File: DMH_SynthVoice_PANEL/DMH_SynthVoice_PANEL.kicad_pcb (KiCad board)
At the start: 2 copper layers, 100 x 200 mm, 5 parts, among them J0 Panel_GND_Solder_Wire_Pad

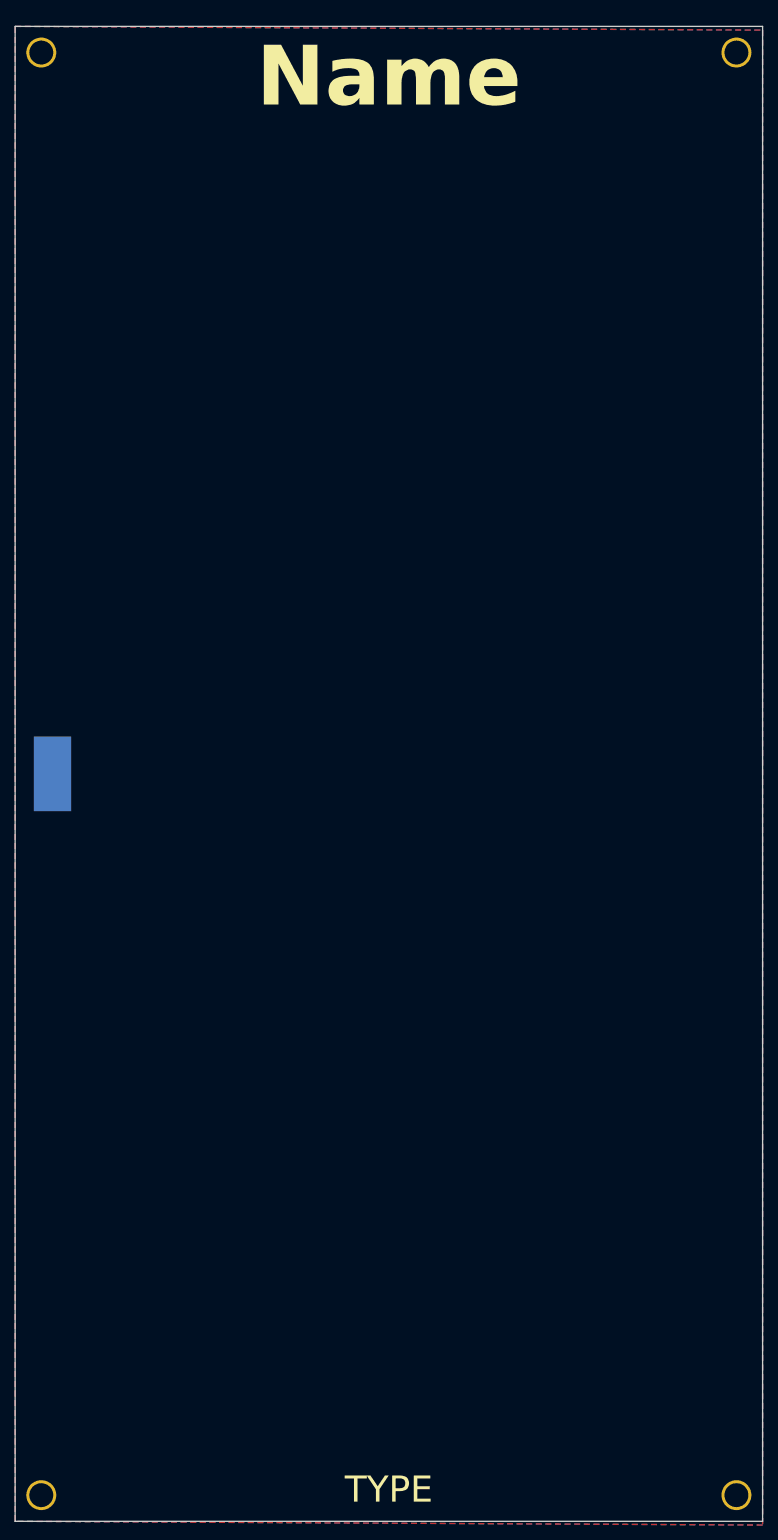
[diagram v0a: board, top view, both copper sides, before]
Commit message: Designed front panel
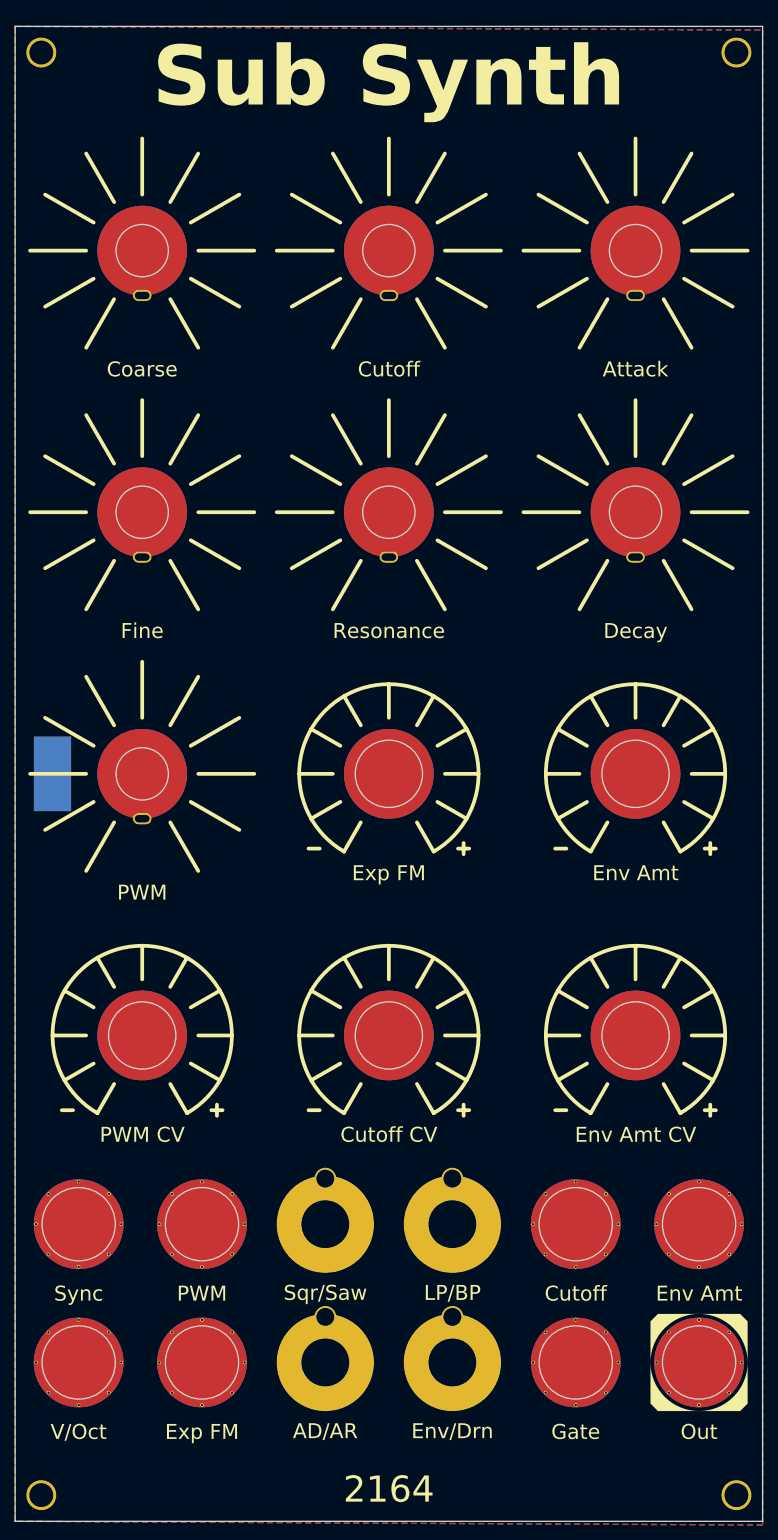
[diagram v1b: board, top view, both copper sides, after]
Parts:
- added H10: Env Amt, SynthStuff:Pot_Cutout_Tiny_attv_P110KH1, F.Cu at (133.0, 130.0)
- added H11: Resonance, SynthStuff:Pot_Cutout_Small, F.Cu at (100.0, 95.0)
- added H12: PWM CV, SynthStuff:Pot_Cutout_Tiny_attv_P110KH1, F.Cu at (67.0, 165.0)
- added H13: Attack, SynthStuff:Pot_Cutout_Small, F.Cu at (133.0, 60.0)
- added H14: Decay, SynthStuff:Pot_Cutout_Small, F.Cu at (133.0, 95.0)
- added H15: Exp FM, SynthStuff:Pot_Cutout_Tiny_attv_P110KH1, F.Cu at (100.0, 130.0)
- added H16: Cutoff CV, SynthStuff:Pot_Cutout_Tiny_attv_P110KH1, F.Cu at (100.0, 165.0)
- added H17: V/Oct, SynthStuff:Jack_6.35mm_Cutout_v3, F.Cu at (58.5, 208.8)
- added H18: Exp FM, SynthStuff:Jack_6.35mm_Cutout_v3, F.Cu at (75.0, 208.8)
- added H19: Cutoff, SynthStuff:Jack_6.35mm_Cutout_v3, F.Cu at (125.0, 190.2)
- added H20: Env Amt, SynthStuff:Jack_6.35mm_Cutout_v3, F.Cu at (141.5, 190.2)
- added H21: PWM, SynthStuff:Jack_6.35mm_Cutout_v3, F.Cu at (75.0, 190.2)
- added H22: Out, SynthStuff:Jack_6.35mm_Cutout_Output_v6, F.Cu at (141.5, 208.8)
- added H23: Sqr/Saw, SynthStuff:Toggle_Switch_TE_Cutout, F.Cu at (91.5, 190.2)
- added H24: LP/BP, SynthStuff:Toggle_Switch_TE_Cutout, F.Cu at (108.5, 190.2)
- added H25: Sync, SynthStuff:Jack_6.35mm_Cutout_v3, F.Cu at (58.5, 190.2)
- added H26: AD/AR, SynthStuff:Toggle_Switch_TE_Cutout, F.Cu at (91.5, 208.8)
- added H27: Env/Drn, SynthStuff:Toggle_Switch_TE_Cutout, F.Cu at (108.5, 208.8)
- added H28: Gate, SynthStuff:Jack_6.35mm_Cutout_v3, F.Cu at (125.0, 208.8)
- added H5: Coarse, SynthStuff:Pot_Cutout_Small, F.Cu at (67.0, 60.0)
- added H6: Fine, SynthStuff:Pot_Cutout_Small, F.Cu at (67.0, 95.0)
- added H7: Env Amt CV, SynthStuff:Pot_Cutout_Tiny_attv_P110KH1, F.Cu at (133.0, 165.0)
- added H8: PWM, SynthStuff:Pot_Cutout_Small, F.Cu at (67.0, 130.0)
- added H9: Cutoff, SynthStuff:Pot_Cutout_Small, F.Cu at (100.0, 60.0)
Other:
- board text added: "2164"
- board text added: "Sub Synth"
- board text removed: "Name"
- board text removed: "TYPE"

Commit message: Matched panel layout to SuperSaw module
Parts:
- H10: value Env Amt -> F.E. Amt; footprint SynthStuff:Pot_Cutout_Tiny_attv_P110KH1 -> SynthStuff:Pot_Cutout_Small_attv_P110KH1
- H11: value Resonance -> Cutoff
- H13: value Attack -> Decay
- H14: value Decay -> Resonance
- H15: value Exp FM -> Cutoff CV
- H16: value Cutoff CV -> Exp FM CV
- H20: value Env Amt -> F.E. Amt
- H24: value LP/BP -> AD/AR
- H26: value AD/AR -> LP/BP
- H27: value Env/Drn -> A.E +/d/-
- H7: value Env Amt CV -> F.E. Amt CV
- H9: value Cutoff -> Attack
